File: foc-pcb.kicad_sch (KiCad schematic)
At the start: 35 parts, among them U5 RBB06DHHN, U6 SPX3819M5-L-5-0

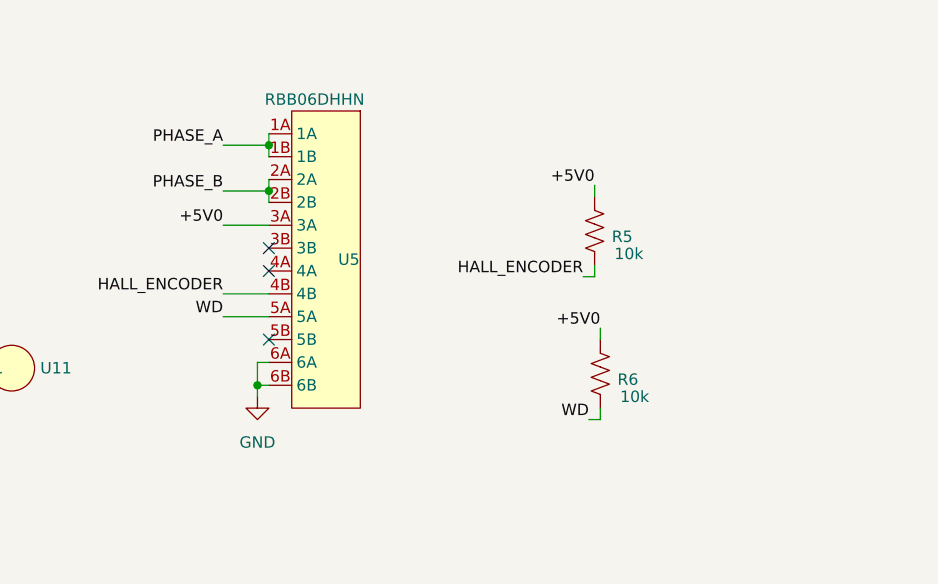
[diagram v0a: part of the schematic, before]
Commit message: switch to 5V excitation for halls which is confirmed working on hardware
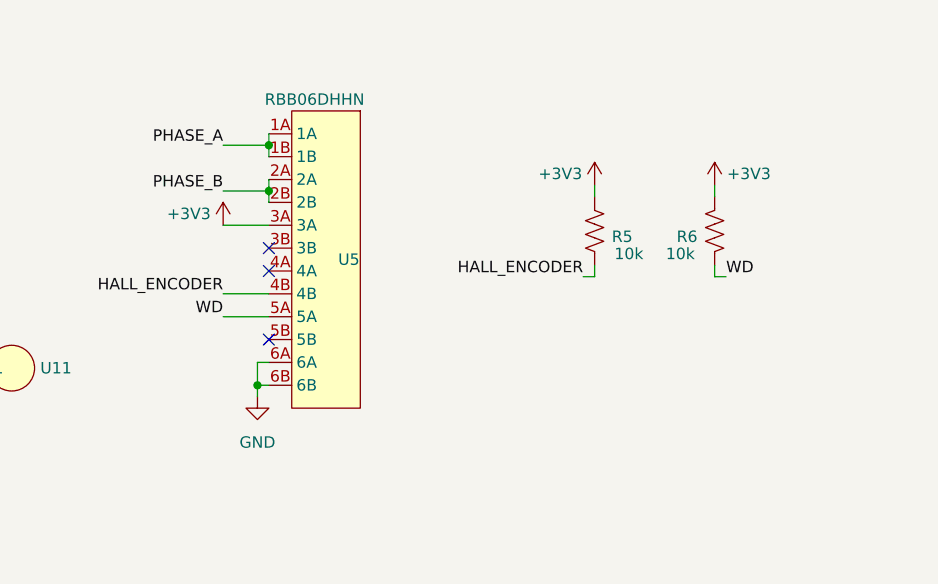
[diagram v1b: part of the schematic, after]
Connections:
- net +3V3: now also R5.1, R6.1, U5.3A
- net +5V0: no longer R5.1, R6.1, U5.3A
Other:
- moved on the sheet: R6
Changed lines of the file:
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@@
     (stroke (width 0) (type default))
   )
-  (wire (pts (xy 264.16 170.815) (xy 264.16 169.545))
+  (wire (pts (xy 276.86 154.94) (xy 276.86 153.67))
     (stroke (width 0) (type default))
   )
@@
     (stroke (width 0) (type default))
   )
-  (wire (pts (xy 264.16 160.655) (xy 264.16 161.925))
+  (wire (pts (xy 276.86 144.78) (xy 276.86 146.05))
     (stroke (width 0) (type default))
   )
@@
     (stroke (width 0) (type default))
   )
-  (wire (pts (xy 262.89 170.815) (xy 264.16 170.815))
+  (wire (pts (xy 278.13 154.94) (xy 276.86 154.94))
     (stroke (width 0) (type default))
   )
@@
     (effects (font (size 1.27 1.27)) (justify right bottom))
   )
-  (label "+5V0" (at 222.25 149.225 180) (fields_autoplaced)
-    (effects (font (size 1.27 1.27)) (justify right bottom))
-  )
-  (label "+5V0" (at 263.525 144.78 180) (fields_autoplaced)
-    (effects (font (size 1.27 1.27)) (justify right bottom))
-  )
   (label "ENABLE" (at 147.32 108.585 180) (fields_autoplaced)
     (effects (font (size 1.27 1.27)) (justify right bottom))
@@
     (effects (font (size 1.27 1.27)) (justify right bottom))
   )
-  (label "+5V0" (at 264.16 160.655 180) (fields_autoplaced)
-    (effects (font (size 1.27 1.27)) (justify right bottom))
-  )
   (label "HALL_ENCODER" (at 95.25 147.32 180) (fields_autoplaced)
     (effects (font (size 1.27 1.27)) (justify right bottom))
@@
     (effects (font (size 1.27 1.27)) (justify right bottom))
   )
-  (label "WD" (at 262.89 170.815 180) (fields_autoplaced)
-    (effects (font (size 1.27 1.27)) (justify right bottom))
+  (label "WD" (at 278.13 154.94 0) (fields_autoplaced)
+    (effects (font (size 1.27 1.27)) (justify left bottom))
   )
   (label "+5V0" (at 212.09 236.855 0) (fields_autoplaced)
@@
     )
   )
+  (symbol (lib_id "power:+3V3") (at 263.525 144.78 0) (unit 1)
+    (in_bom yes) (on_board yes) (dnp no)
+    (property "Reference" "#PWR021" (at 263.525 148.59 0)
+      (effects (font (size 1.27 1.27)) hide)
+    )
+    (property "Value" "+3V3" (at 259.715 143.51 0)
+      (effects (font (size 1.27 1.27)))
+    )
+    (property "Footprint" "" (at 263.525 144.78 0)
+      (effects (font (size 1.27 1.27)) hide)
+    )
+    (property "Datasheet" "" (at 263.525 144.78 0)
+      (effects (font (size 1.27 1.27)) hide)
+    )
+    (pin "1")
+    (instances
+      (project "foc-pcb"
+        (path "/2b52ab19-a93e-4439-8602-a1380e4825c0"
+          (reference "#PWR021") (unit 1)
+        )
+      )
+    )
+  )
   (symbol (lib_id "power:GND") (at 248.92 115.57 0) (unit 1)
     (in_bom yes) (on_board yes) (dnp no) (fields_autoplaced)
@@
     )
   )
+  (symbol (lib_id "power:+3V3") (at 276.86 144.78 0) (mirror y) (unit 1)
+    (in_bom yes) (on_board yes) (dnp no)
+    (property "Reference" "#PWR023" (at 276.86 148.59 0)
+      (effects (font (size 1.27 1.27)) hide)
+    )
+    (property "Value" "+3V3" (at 280.67 143.51 0)
+      (effects (font (size 1.27 1.27)))
+    )
+    (property "Footprint" "" (at 276.86 144.78 0)
+      (effects (font (size 1.27 1.27)) hide)
+    )
+    (property "Datasheet" "" (at 276.86 144.78 0)
+      (effects (font (size 1.27 1.27)) hide)
+    )
+    (pin "1")
+    (instances
+      (project "foc-pcb"
+        (path "/2b52ab19-a93e-4439-8602-a1380e4825c0"
+          (reference "#PWR023") (unit 1)
+        )
+      )
+    )
+  )
   (symbol (lib_id "power:GND") (at 299.72 115.57 0) (unit 1)
     (in_bom yes) (on_board yes) (dnp no) (fields_autoplaced)
@@
     )
   )
-  (symbol (lib_id "foc-pcb-lib:Resistor") (at 264.16 165.735 0) (unit 1)
-    (in_bom yes) (on_board yes) (dnp no)
-    (property "Reference" "R6" (at 266.065 166.37 0)
-      (effects (font (size 1.27 1.27)) (justify left))
-    )
-    (property "Value" "10k" (at 267.97 168.275 0)
-      (effects (font (size 1.27 1.27)))
-    )
-    (property "Footprint" "foc-pcb-library:R_0402_1005Metric" (at 259.08 153.035 0)
-      (effects (font (size 1.27 1.27)) hide)
-    )
-    (property "Datasheet" "~" (at 264.16 165.735 0)
+  (symbol (lib_id "foc-pcb-lib:Resistor") (at 276.86 149.86 0) (mirror y) (unit 1)
+    (in_bom yes) (on_board yes) (dnp no)
+    (property "Reference" "R6" (at 274.955 150.495 0)
+      (effects (font (size 1.27 1.27)) (justify left))
+    )
+    (property "Value" "10k" (at 273.05 152.4 0)
+      (effects (font (size 1.27 1.27)))
+    )
+    (property "Footprint" "foc-pcb-library:R_0402_1005Metric" (at 281.94 137.16 0)
+      (effects (font (size 1.27 1.27)) hide)
+    )
+    (property "Datasheet" "~" (at 276.86 149.86 0)
       (effects (font (size 1.27 1.27)) hide)
     )
@@
         )
       )
+    )
+  )
+  (symbol (lib_id "power:+3V3") (at 222.25 149.225 0) (unit 1)
+    (in_bom yes) (on_board yes) (dnp no)
+    (property "Reference" "#PWR020" (at 222.25 153.035 0)
+      (effects (font (size 1.27 1.27)) hide)
+    )
+    (property "Value" "+3V3" (at 218.44 147.955 0)
+      (effects (font (size 1.27 1.27)))
+    )
+    (property "Footprint" "" (at 222.25 149.225 0)
+      (effects (font (size 1.27 1.27)) hide)
+    )
+    (property "Datasheet" "" (at 222.25 149.225 0)
+      (effects (font (size 1.27 1.27)) hide)
+    )
+    (pin "1")
+    (instances
+      (project "foc-pcb"
+        (path "/2b52ab19-a93e-4439-8602-a1380e4825c0"
+          (reference "#PWR020") (unit 1)
+        )
+      )
